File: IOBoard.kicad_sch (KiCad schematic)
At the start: 29 parts, among them J12 DE9_Receptacle, J13 DE9_Plug, J14 DE9_Receptacle, J15 DE9_Receptacle, J16 DE9_Receptacle, J3 Conn_01x03, J4 Conn_01x03, J5 Conn_01x03, J6 Conn_01x03, J7 Conn_01x03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

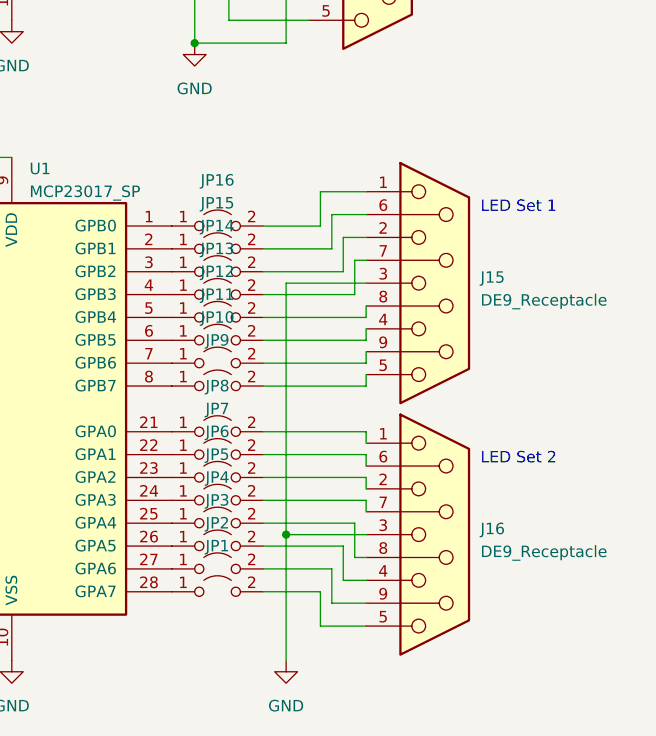
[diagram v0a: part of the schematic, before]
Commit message: Update schematic and PCB to use resistor symbols instead of jumpers.
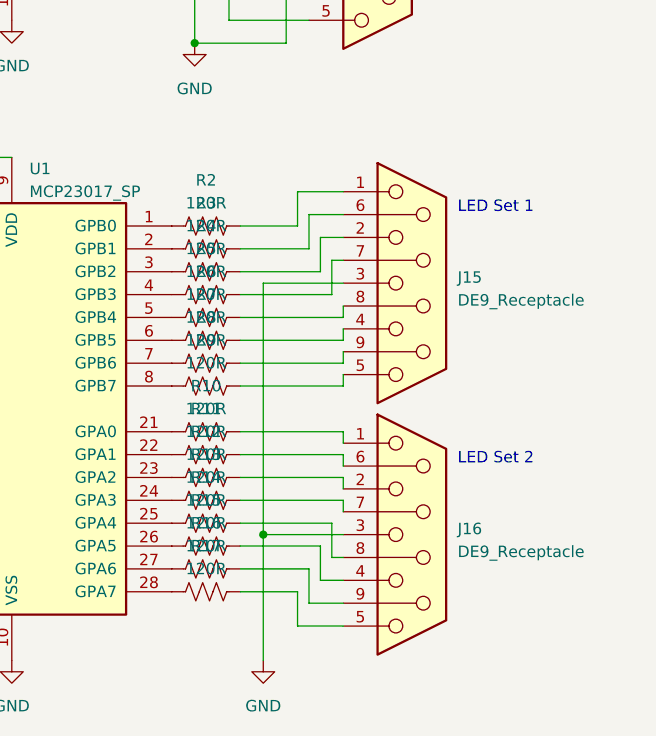
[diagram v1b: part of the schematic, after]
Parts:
- removed JP1, JP10, JP11, JP12, JP13, JP14, JP15, JP16, JP2, JP3, JP4, JP5, JP6, JP7, JP8, JP9: Jumper_2_Open, Resistor_THT:R_Axial_DIN0207_L6.3mm_D2.5mm_P10.16mm_Horizontal, symbol Jumper:Jumper_2_Open
- added R10, R11, R12, R13, R14, R15, R16, R17, R2, R3, R4, R5, R6, R7, R8, R9: 120R, Resistor_THT:R_Axial_DIN0207_L6.3mm_D2.5mm_P7.62mm_Horizontal, symbol Device:R_US
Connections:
- net at U1.4 (GPB3): now also R5.2
- net at J15.7: now also R5.1
- net at U1.27 (GPA6): now also R16.2
- net at J16.9: now also R16.1
- net at U1.22 (GPA1): now also R11.2
- net at J16.6: now also R11.1
- net at U1.7 (GPB6): now also R8.2
- net at J15.9: now also R8.1
- net at U1.25 (GPA4): now also R14.2
- net at J16.8: now also R14.1
- net at U1.28 (GPA7): now also R17.2
- net at J16.5: now also R17.1
- net at U1.24 (GPA3): now also R13.2
- net at J16.7: now also R13.1
- net at J16.1: now also R10.1
- net at J16.2: now also R12.1
- net at J16.4: now also R15.1
- net at J15.1: now also R2.1
- net at J15.2: now also R4.1
- net at J15.4: now also R7.1
- net at J15.5: now also R9.1
- net at J15.6: now also R3.1
- net at J15.8: now also R6.1
- net at U1.5 (GPB4): now also R6.2
- net at U1.6 (GPB5): now also R7.2
- net at U1.8 (GPB7): now also R9.2
- net at U1.23 (GPA2): now also R12.2
- net at U1.1 (GPB0): now also R2.2
- net at U1.2 (GPB1): now also R3.2
- net at U1.21 (GPA0): now also R10.2
- net at U1.26 (GPA5): now also R15.2
- net at U1.3 (GPB2): now also R4.2
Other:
- moved on the sheet: J15, J16

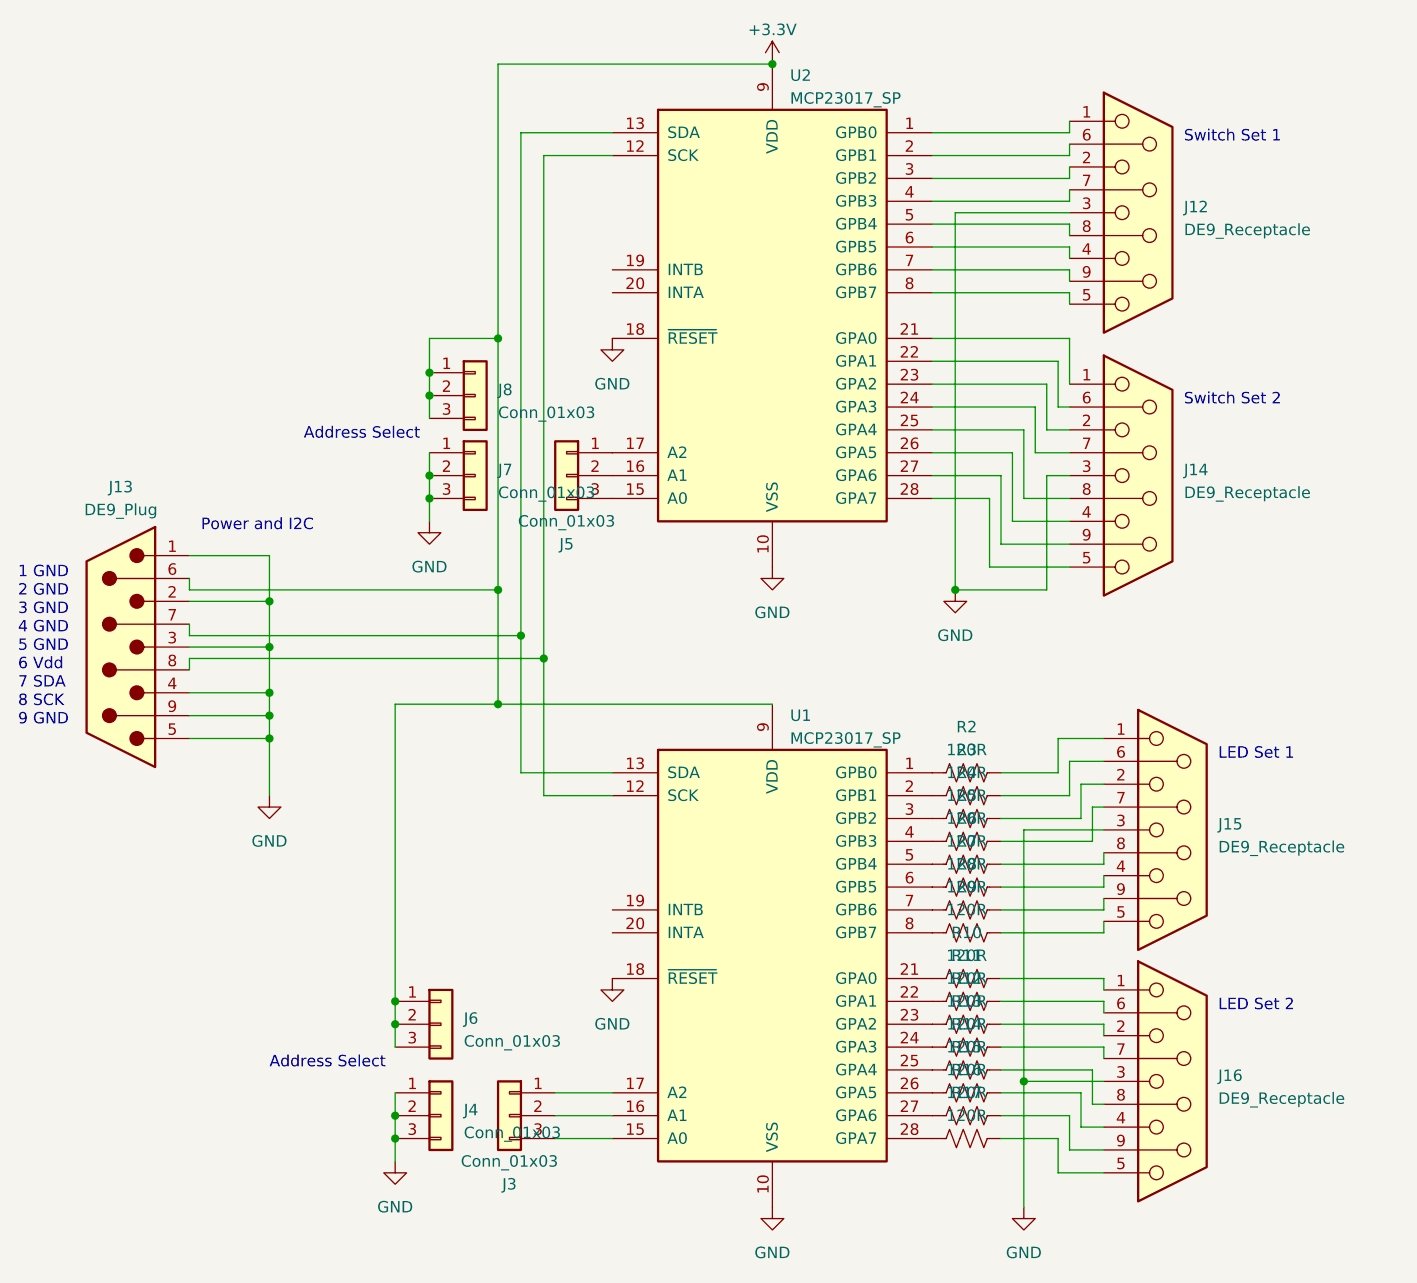
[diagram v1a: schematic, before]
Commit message: Update PCB to use SMD resistors and rectangular connectors.  This lets the PCB shrink some more and it may be easier to crimp rectangular connectors onto ribbon cable than to solder a bunch of D-9 connectors.
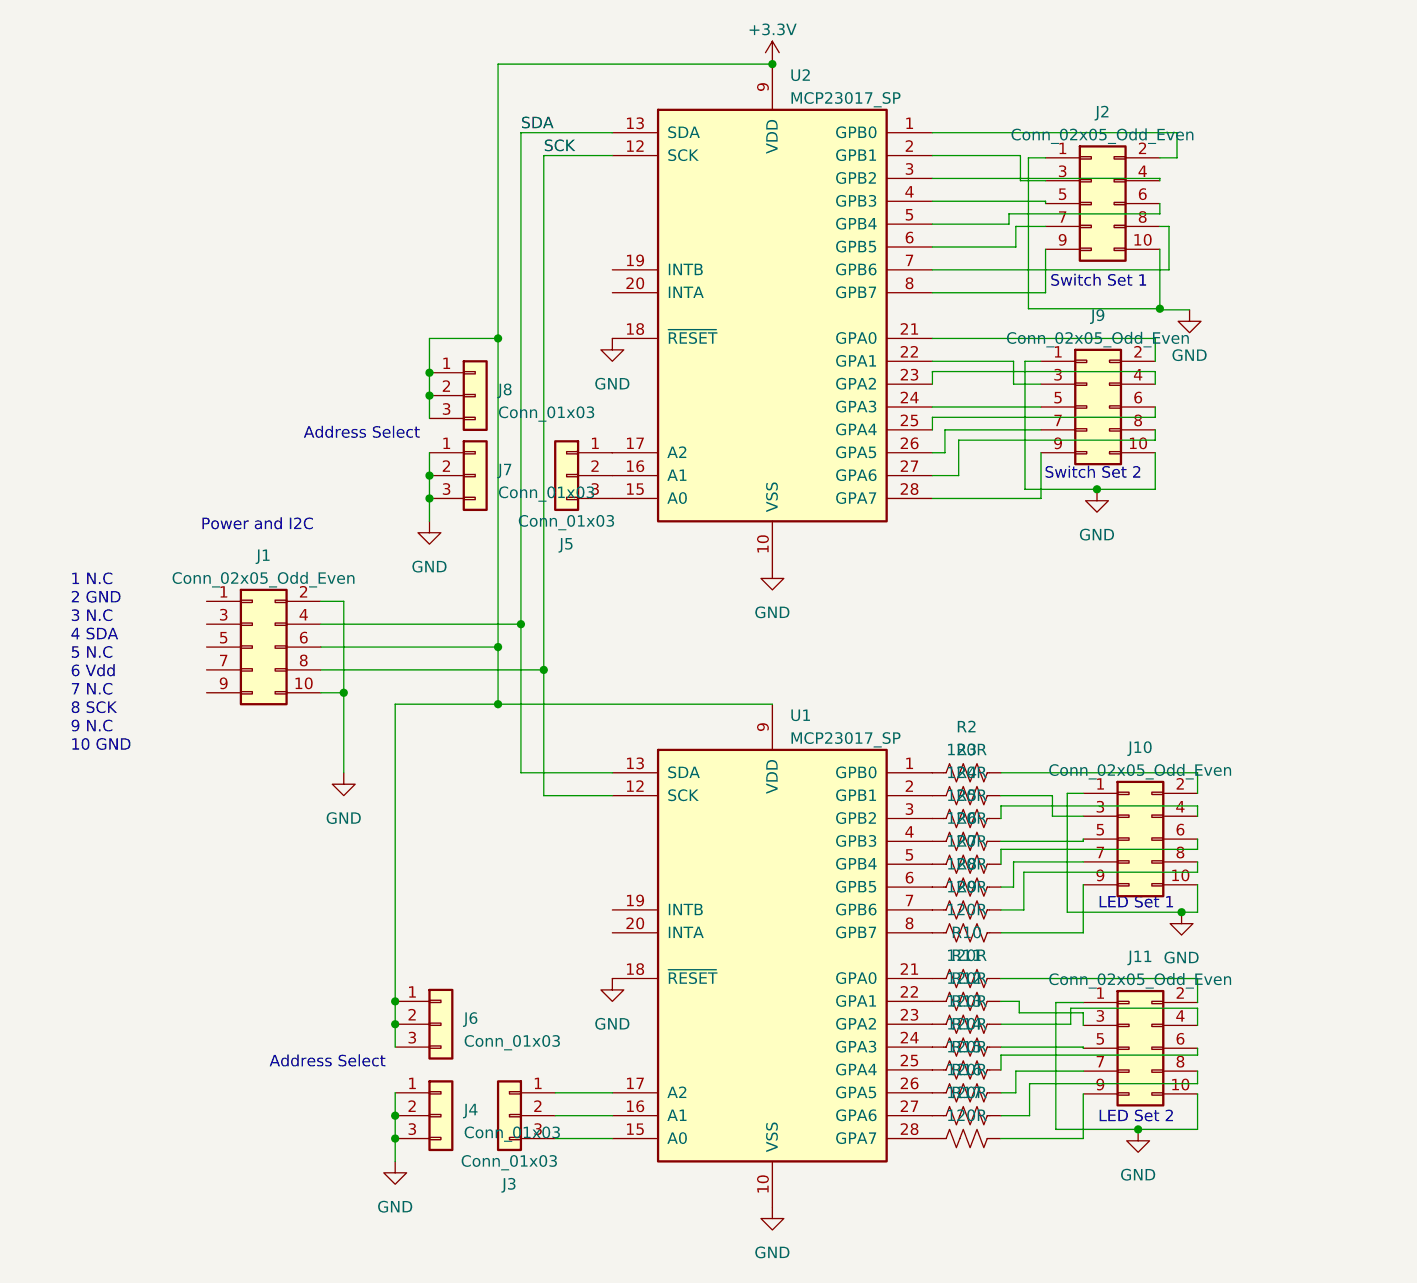
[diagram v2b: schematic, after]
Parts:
- removed J12, J14, J15, J16: DE9_Receptacle, Connector_Dsub:DSUB-9_Female_Vertical_P2.77x2.84mm, symbol Connector:DE9_Receptacle
- removed J13: DE9_Plug, Connector_Dsub:DSUB-9_Male_Horizontal_P2.77x2.84mm_EdgePinOffset4.94mm_Housed_MountingHolesOffset7.48mm, symbol Connector:DE9_Plug
- added J1: Conn_02x05_Odd_Even, Connector_PinHeader_2.54mm:PinHeader_2x05_P2.54mm_Horizontal, symbol Connector_Generic:Conn_02x05_Odd_Even
- added J10, J11, J2, J9: Conn_02x05_Odd_Even, Connector_PinHeader_2.54mm:PinHeader_2x05_P2.54mm_Vertical, symbol Connector_Generic:Conn_02x05_Odd_Even
- R10, R11, R12, R13, R14, R15, R16, R17, R2, R3, R4, R5, R6, R7, R8, R9: footprint Resistor_THT:R_Axial_DIN0207_L6.3mm_D2.5mm_P7.62mm_Horizontal -> Resistor_SMD:R_1206_3216Metric_Pad1.30x1.75mm_HandSolder
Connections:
- net +3.3V: now also J1.6 (Pin_6)
- net GND: now also J1.10 (Pin_10), J1.2 (Pin_2), J10.1 (Pin_1), J10.10 (Pin_10), J11.1 (Pin_1), J11.10 (Pin_10), J2.1 (Pin_1), J2.10 (Pin_10), J9.1 (Pin_1), J9.10 (Pin_10)
- net at R2.1: now also J10.2 (Pin_2)
- net at R4.1: now also J10.4 (Pin_4)
- net at R11.1: now also J11.3 (Pin_3)
- net at U2.1 (GPB0): now also J2.2 (Pin_2)
- net SCK: now reaches U1.12 (SCK), U2.12 (SCK)
- net SCK: now also J1.8 (Pin_8)
- net SDA: now reaches U1.13 (SDA), U2.13 (SDA)
- net SDA: now also J1.4 (Pin_4)
- net at U2.2 (GPB1): now also J2.3 (Pin_3)
- net at U2.21 (GPA0): now also J9.2 (Pin_2)
- net at U2.22 (GPA1): now also J9.3 (Pin_3)
- net at U2.23 (GPA2): now also J9.4 (Pin_4)
- net at U2.24 (GPA3): now also J9.5 (Pin_5)
- net at U2.25 (GPA4): now also J9.6 (Pin_6)
- net at U2.26 (GPA5): now also J9.7 (Pin_7)
- net at U2.27 (GPA6): now also J9.8 (Pin_8)
- net at U2.28 (GPA7): now also J9.9 (Pin_9)
- net at U2.3 (GPB2): now also J2.4 (Pin_4)
- net at U2.4 (GPB3): now also J2.5 (Pin_5)
- net at U2.5 (GPB4): now also J2.6 (Pin_6)
- net at U2.6 (GPB5): now also J2.7 (Pin_7)
- net at U2.7 (GPB6): now also J2.8 (Pin_8)
- net at U2.8 (GPB7): now also J2.9 (Pin_9)
- net at R8.1: now also J10.8 (Pin_8)
- net at R7.1: now also J10.7 (Pin_7)
- net at R16.1: now also J11.8 (Pin_8)
- net at R10.1: now also J11.2 (Pin_2)
- net at R12.1: now also J11.4 (Pin_4)
- net at R15.1: now also J11.7 (Pin_7)
- net at R17.1: now also J11.9 (Pin_9)
- net at R13.1: now also J11.5 (Pin_5)
- net at R14.1: now also J11.6 (Pin_6)
- net at R6.1: now also J10.6 (Pin_6)
- net at R9.1: now also J10.9 (Pin_9)
- net at R3.1: now also J10.3 (Pin_3)
- net at R5.1: now also J10.5 (Pin_5)
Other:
- note added: "1 N.C 2 GND 3 N.C 4 SDA 5 N.C 6 Vdd 7 N.C 8 SCK 9 N.C 10 GND"
- note removed: "1 GND 2 GND 3 GND 4 GND 5 GND 6 Vdd 7 SDA 8 SCK 9 GND"

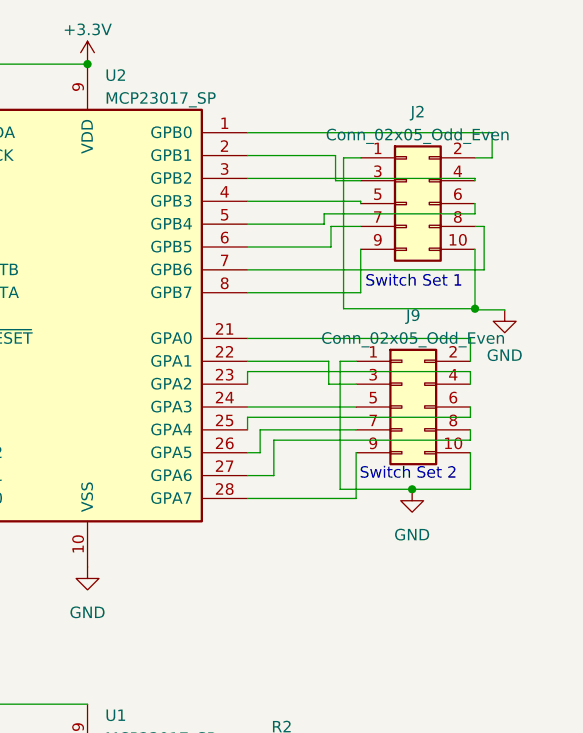
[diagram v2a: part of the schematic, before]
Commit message: Update schematic to add resisters on inputs as well.  Submitted PCB for production.  Once PCBs are received, assembled, tested, and working, I'll update documentation.
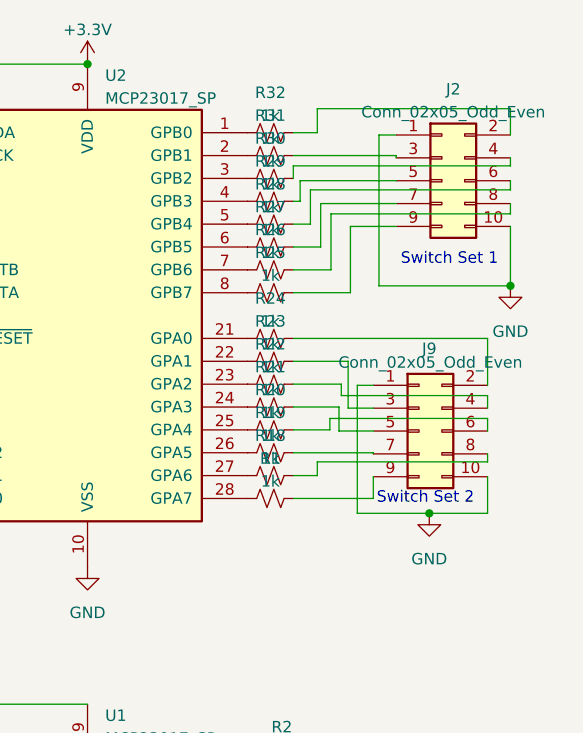
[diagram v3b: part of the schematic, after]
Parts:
- added R1, R18, R19, R20, R21, R22, R23, R24, R25, R26, R27, R28, R29, R30, R31, R32: 1k, Resistor_SMD:R_1206_3216Metric_Pad1.30x1.75mm_HandSolder, symbol Device:R_Small_US
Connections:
- net at J9.2 (Pin_2): now also R24.2; no longer U2.21 (GPA0)
- net at J9.3 (Pin_3): now also R23.2; no longer U2.22 (GPA1)
- net at J9.4 (Pin_4): now also R22.2; no longer U2.23 (GPA2)
- net at J9.5 (Pin_5): now also R21.2; no longer U2.24 (GPA3)
- net at J9.6 (Pin_6): now also R20.2; no longer U2.25 (GPA4)
- net at J9.7 (Pin_7): now also R19.2; no longer U2.26 (GPA5)
- net at J9.8 (Pin_8): now also R18.2; no longer U2.27 (GPA6)
- net at J9.9 (Pin_9): now also R1.2; no longer U2.28 (GPA7)
- net at U2.1 (GPB0): now also R32.1; no longer J2.2 (Pin_2)
- net at U2.2 (GPB1): now also R31.1; no longer J2.3 (Pin_3)
- net at U2.3 (GPB2): now also R30.1; no longer J2.4 (Pin_4)
- net at U2.4 (GPB3): now also R29.1; no longer J2.5 (Pin_5)
- net at U2.5 (GPB4): now also R28.1; no longer J2.6 (Pin_6)
- net at U2.6 (GPB5): now also R27.1; no longer J2.7 (Pin_7)
- net at U2.7 (GPB6): now also R26.1; no longer J2.8 (Pin_8)
- net at U2.8 (GPB7): now also R25.1; no longer J2.9 (Pin_9)
- new net: J2.9 (Pin_9), R25.2
- new net: R24.1, U2.21 (GPA0)
- new net: R23.1, U2.22 (GPA1)
- new net: R22.1, U2.23 (GPA2)
- new net: R21.1, U2.24 (GPA3)
- new net: R20.1, U2.25 (GPA4)
- new net: R19.1, U2.26 (GPA5)
- new net: R18.1, U2.27 (GPA6)
- new net: R1.1, U2.28 (GPA7)
- new net: J2.8 (Pin_8), R26.2
- new net: J2.6 (Pin_6), R28.2
- new net: J2.5 (Pin_5), R29.2
- new net: J2.2 (Pin_2), R32.2
- new net: J2.4 (Pin_4), R30.2
- new net: J2.7 (Pin_7), R27.2
- new net: J2.3 (Pin_3), R31.2
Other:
- moved on the sheet: J2, J9
